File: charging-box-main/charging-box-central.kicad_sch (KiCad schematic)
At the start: 15 parts, among them J1 Accumulator 1, J10 mains power indicator, J11 Close AIRs, J2 Accumulator 2, J3 Main 12V, J4 Latching, J5 Charger, J6 IMD FAULT LED active low, J7 BMS LED active low, J8 Latching reset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

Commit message: mounting holes and rounded corners
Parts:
- added H1, H2, H3, H4: MountingHole_Pad, MountingHole:MountingHole_3.2mm_M3_DIN965_Pad_TopBottom, symbol Mechanical:MountingHole_Pad
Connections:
- net GND: now also H1.1, H2.1, H3.1, H4.1

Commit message: put the labels
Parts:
- R1, R2, R7: footprint Resistor_THT:R_Axial_DIN0207_L6.3mm_D2.5mm_P10.16mm_Horizontal -> Resistor_SMD:R_0805_2012Metric_Pad1.20x1.40mm_HandSolder
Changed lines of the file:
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@@
 			)
 		)
-		(property "Footprint" "Resistor_THT:R_Axial_DIN0207_L6.3mm_D2.5mm_P10.16mm_Horizontal"
+		(property "Footprint" "Resistor_SMD:R_0805_2012Metric_Pad1.20x1.40mm_HandSolder"
 			(at 125.095 134.112 90)
 			(effects
@@
 			)
 		)
-		(property "Footprint" "Resistor_THT:R_Axial_DIN0207_L6.3mm_D2.5mm_P10.16mm_Horizontal"
+		(property "Footprint" "Resistor_SMD:R_0805_2012Metric_Pad1.20x1.40mm_HandSolder"
 			(at 180.34 84.328 90)
 			(effects
@@
 			)
 		)
-		(property "Footprint" "Resistor_THT:R_Axial_DIN0207_L6.3mm_D2.5mm_P10.16mm_Horizontal"
+		(property "Footprint" "Resistor_SMD:R_0805_2012Metric_Pad1.20x1.40mm_HandSolder"
 			(at 180.34 91.313 90)
 			(effects

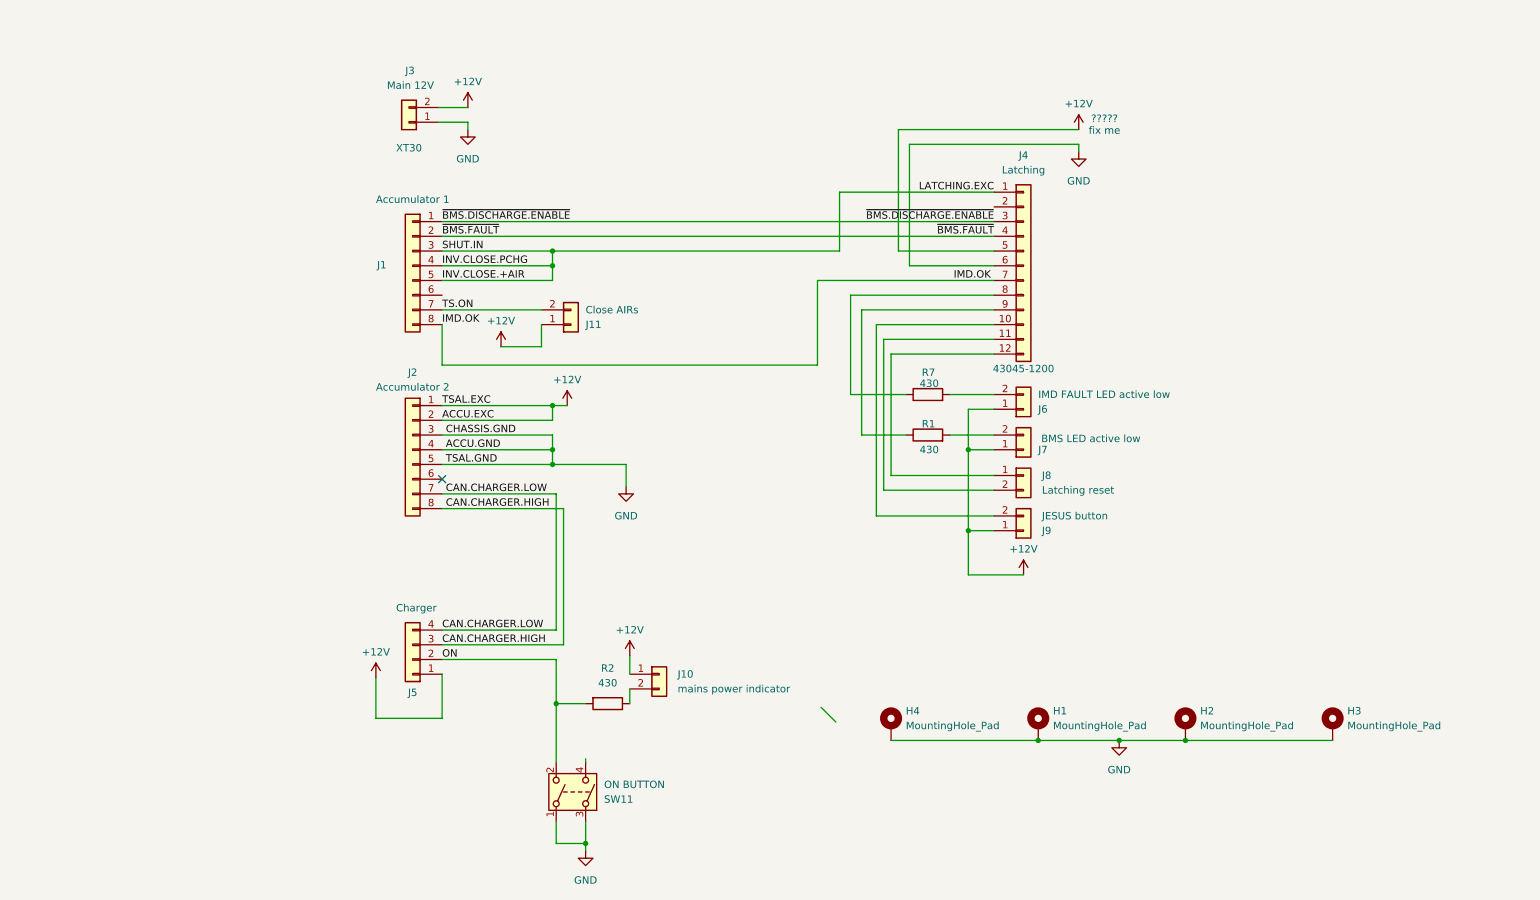
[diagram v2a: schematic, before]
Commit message: added fuses
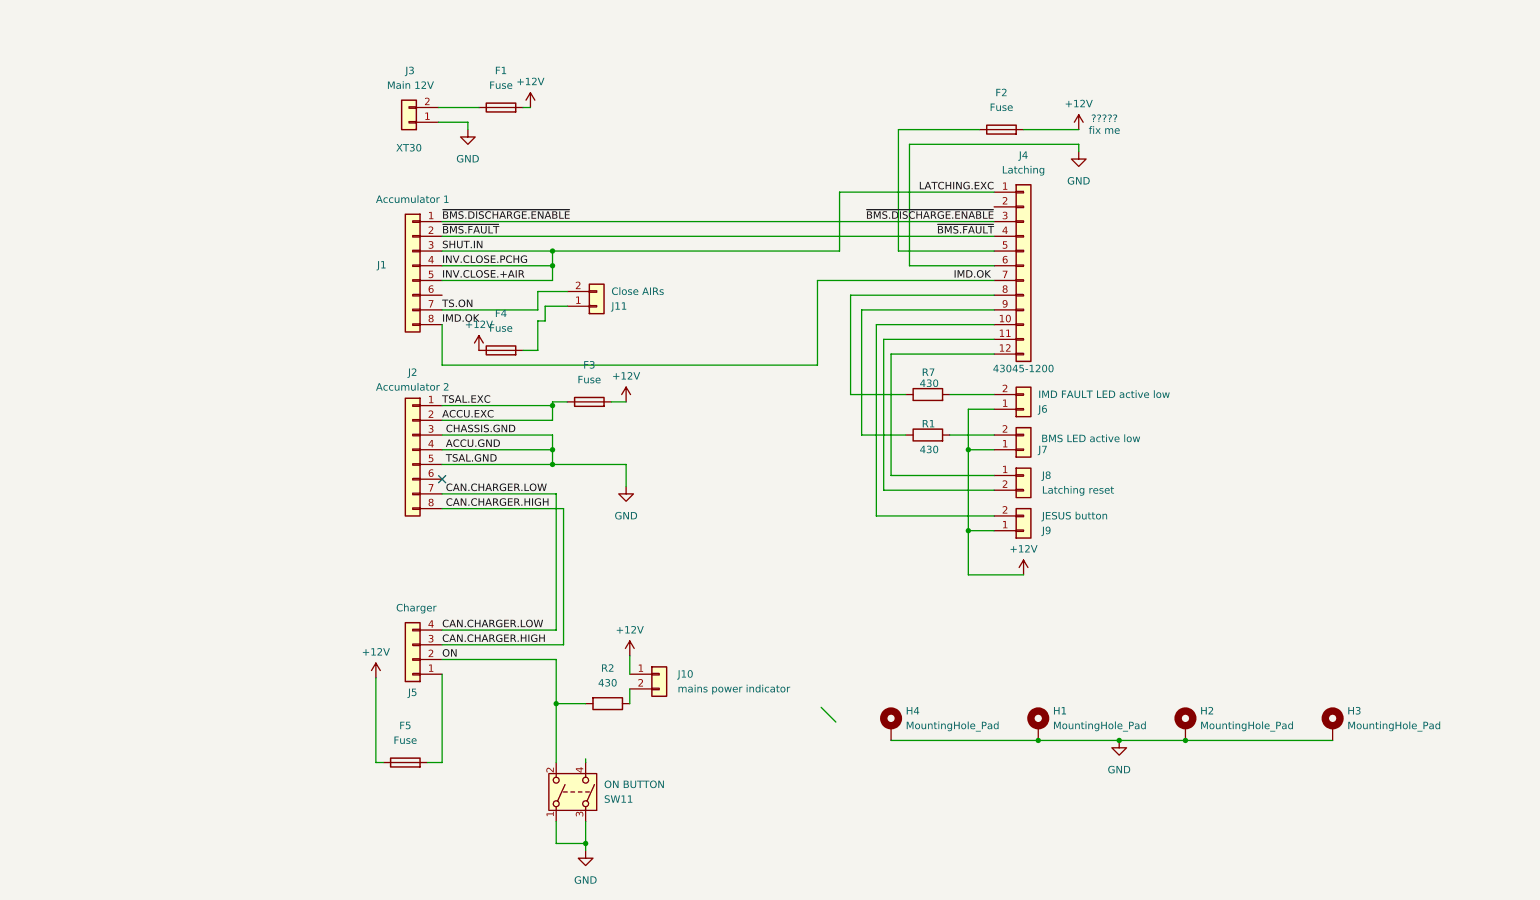
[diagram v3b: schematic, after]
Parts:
- added F1, F2, F3, F4, F5: Fuse, Fuse:Fuse_0603_1608Metric, symbol Device:Fuse
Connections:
- net +12V: now also F1.2, F2.2, F3.2, F4.1, F5.1; no longer J11.1 (Pin_1), J2.1 (Pin_1), J2.2 (Pin_2), J3.2 (Pin_2), J4.5 (Pin_5), J5.1 (Pin_1)
- new net: F2.1, J4.5 (Pin_5)
- new net: F4.2, J11.1 (Pin_1)
- new net: F5.2, J5.1 (Pin_1)
- new net: F1.1, J3.2 (Pin_2)
- new net ACCU.EXC: F3.1, J2.1 (Pin_1), J2.2 (Pin_2)
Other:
- moved on the sheet: J11

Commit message: made it a lill bit neater
not much
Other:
- note added: "????? fix me no"
- note removed: "????? fix me"
- moved on the sheet: F1, F2, F3, F4, F5, J1, J10, J11, J2, J3, J4, J5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

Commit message: routing fixes
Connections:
- net CAN.CHARGER.HIGH renamed CAN.CHARGER+
- net CAN.CHARGER.LOW renamed CAN.CHARGER-
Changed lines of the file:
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@@
 		)
 	)
-	(label "CAN.CHARGER.LOW"
+	(label "CAN.CHARGER-"
 		(at 67.31 98.425 0)
 		(effects
@@
 		)
 	)
-	(label "CAN.CHARGER.HIGH"
+	(label "CAN.CHARGER+"
 		(at 66.675 124.46 0)
 		(effects
@@
 		)
 	)
-	(label "CAN.CHARGER.LOW"
+	(label "CAN.CHARGER-"
 		(at 66.675 121.92 0)
 		(effects
@@
 		)
 	)
-	(label "CAN.CHARGER.HIGH"
+	(label "CAN.CHARGER+"
 		(at 67.31 100.965 0)
 		(effects

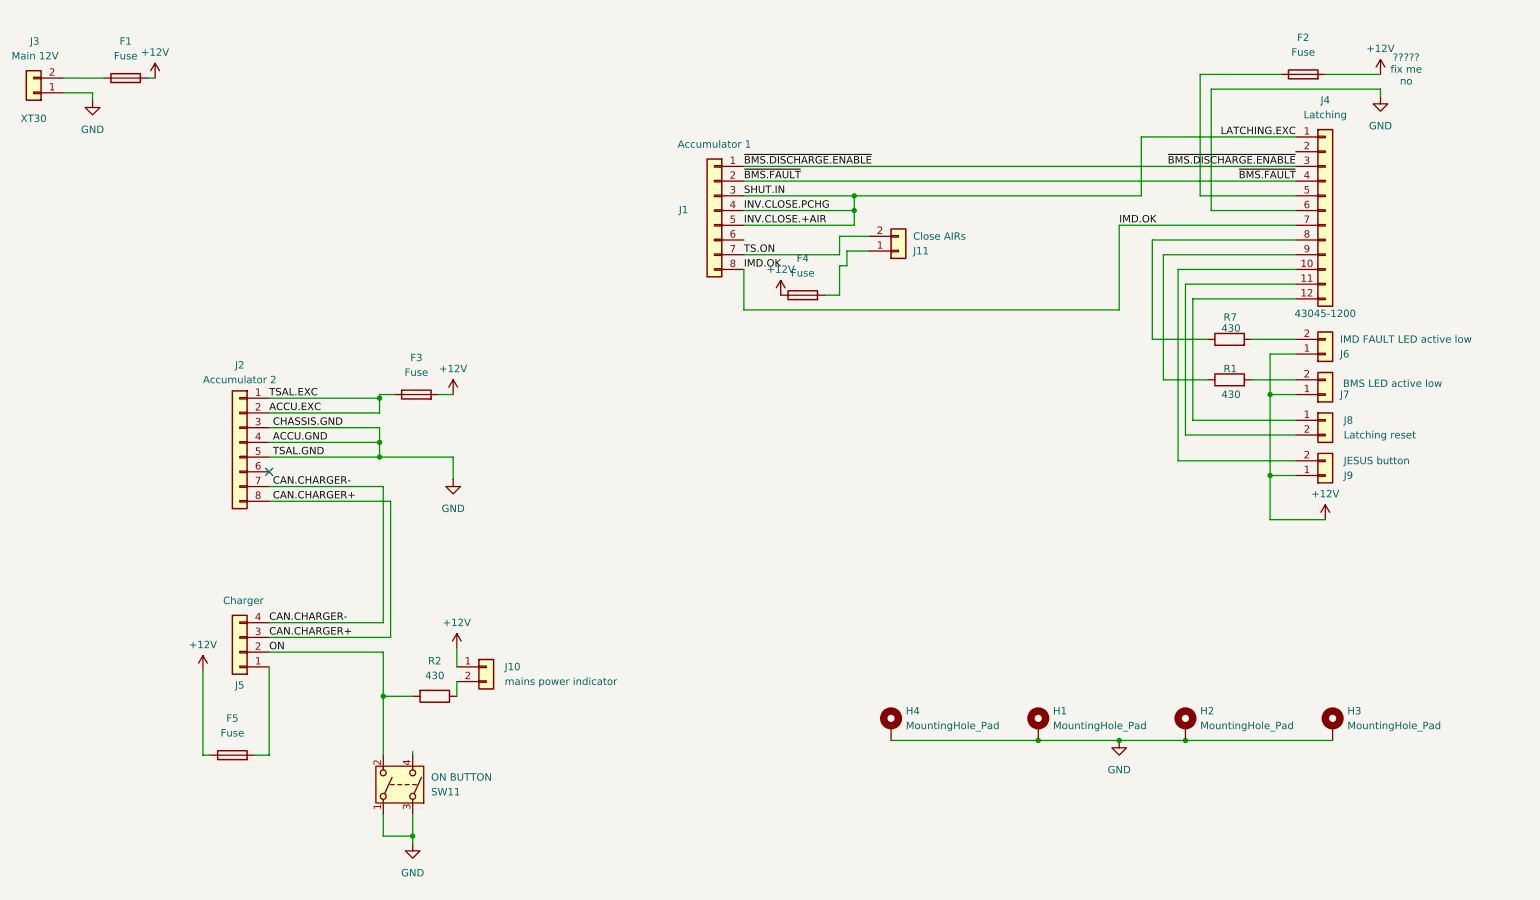
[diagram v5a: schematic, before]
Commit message: Sent pcb for production
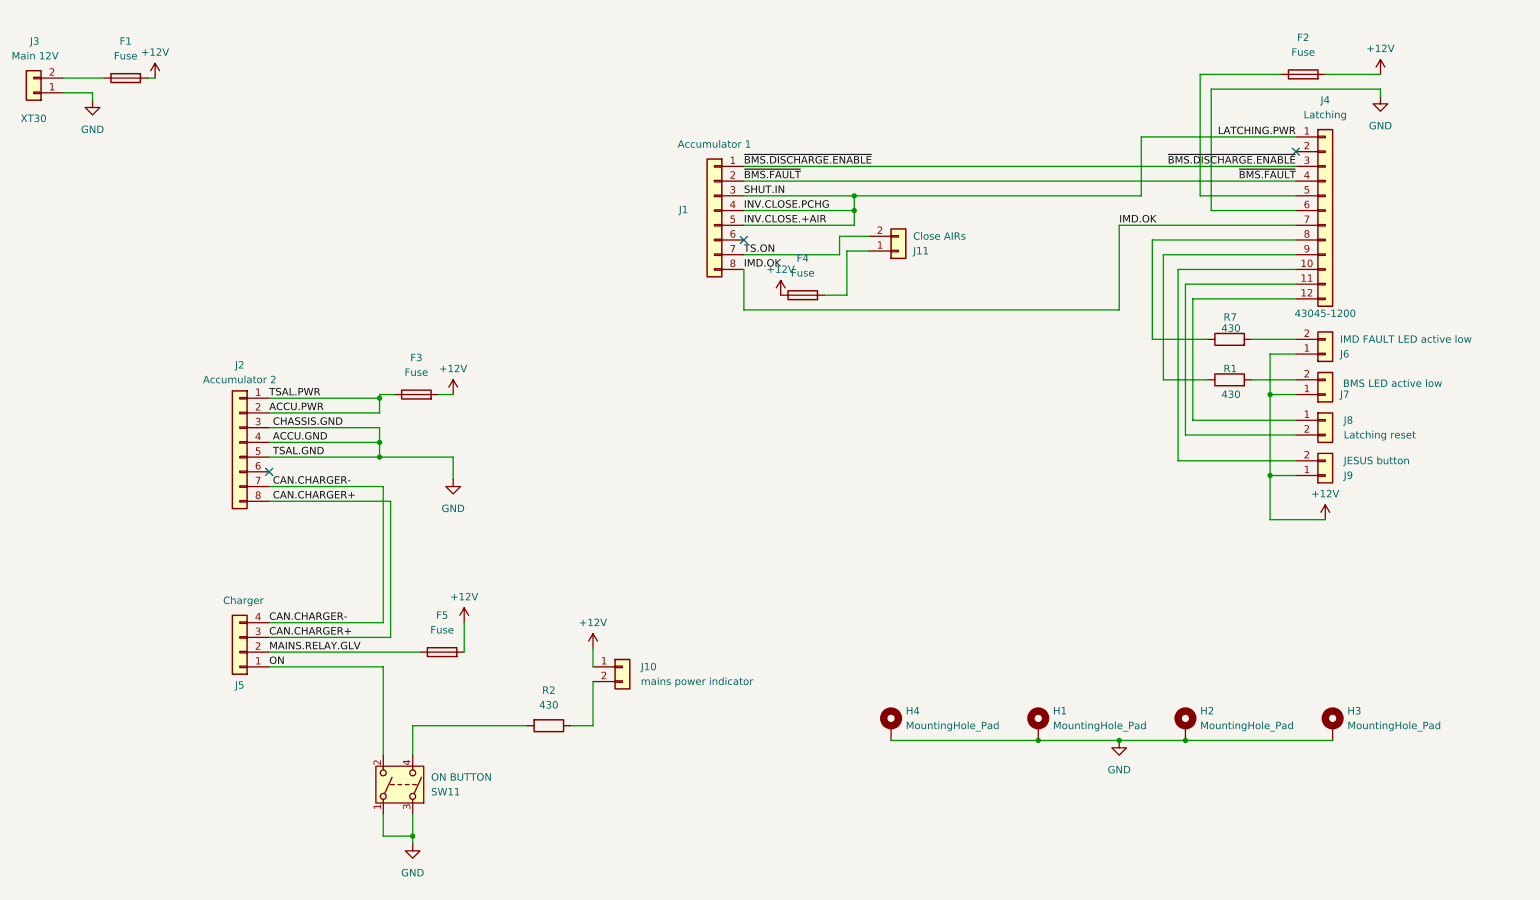
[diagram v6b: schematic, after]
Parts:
- SW11: footprint Connector_Molex:Molex_Micro-Fit_3.0_43045-0200_2x01_P3.00mm_Horizontal -> Connector_Molex:Molex_Micro-Fit_3.0_43045-0400_2x02_P3.00mm_Horizontal
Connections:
- net +12V: now also F5.2; no longer F5.1
- net ON: now also J5.1 (Pin_1); no longer J5.2 (Pin_2), R2.2
- net at SW11.4: now also R2.2
- net ACCU.EXC renamed ACCU.PWR
- new net MAINS.RELAY.GLV: F5.1, J5.2 (Pin_2)
- no-connect marks 1 -> 3
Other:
- note removed: "????? fix me no"
- moved on the sheet: F5, J10, R2

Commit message: Changes
Production on pause
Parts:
- removed F2: Fuse, Fuse:Fuse_0603_1608Metric, symbol Device:Fuse
- added J12: TSAL GREEN LED active high, Connector_Molex:Molex_Micro-Fit_3.0_43045-0200_2x01_P3.00mm_Horizontal, symbol Connector_Generic:Conn_01x02
- added R3: 430, Resistor_SMD:R_0805_2012Metric_Pad1.20x1.40mm_HandSolder, symbol Device:R
- J7: value BMS LED active low -> AMS LED active low
- J9: value JESUS button -> E-STOP
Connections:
- net +12V: now also J4.5 (Pin_5)
- net GND: now also J2.6 (Pin_6), J12.1 (Pin_1); no longer J2.3 (Pin_3)
- net LATCHING.RESET-: now reaches J4.12 (Pin_12), J8.1 (Pin_1)
- net LATCHING.RESET+: now reaches J4.11 (Pin_11), J8.2 (Pin_2)
- net SHUT.LATCHING: now reaches J4.10 (Pin_10), J9.2 (Pin_2)
- net IMD.FAULT.LATCHING: now reaches J4.8 (Pin_8), R7.1
- net AMS.FAULT.LATCHING: now reaches J4.9 (Pin_9), R1.1
- net TSAL.GREEN.LIGHT: now reaches J1.6 (Pin_6)
- net TSAL.GREEN.LIGHT: now also R3.1
- net ACCU.PWR renamed ACCU.CHARGE.PWR
- net ACCU.CHARGE.PWR: now also J2.3 (Pin_3)
- new net: J12.2 (Pin_2), R3.2
- no-connect marks 3 -> 1
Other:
- moved on the sheet: J11

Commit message: add mosfet for green light
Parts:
- added Q1: Q_PMOS-E_Generic_GSD, Package_TO_SOT_SMD:SOT-23, symbol PCM_Transistor_MOSFET_AKL:Q_PMOS-E_Generic_GSD
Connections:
- net +12V: now also Q1.2 (S)
- net TSAL.GREEN.LIGHT: now also Q1.3 (D); no longer J1.6 (Pin_6)
- new net: J1.6 (Pin_6), Q1.1 (G)
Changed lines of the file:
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@@
 	(wire
 		(pts
-			(xy 199.39 113.03) (xy 234.95 113.03)
-		)
-		(stroke
-			(width 0)
-			(type default)
-		)
-	)
-	(wire
-		(pts
 			(xy 243.84 63.5) (xy 224.79 63.5)
 		)
@@
 	(wire
 		(pts
-			(xy 199.39 55.88) (xy 199.39 113.03)
+			(xy 196.85 55.88) (xy 196.85 95.885)
 		)
 		(stroke
@@
 	(wire
 		(pts
+			(xy 205.74 113.03) (xy 205.74 102.235)
+		)
+		(stroke
+			(width 0)
+			(type default)
+		)
+	)
+	(wire
+		(pts
 			(xy 219.075 55.88) (xy 243.84 55.88)
 		)
@@
 	(wire
 		(pts
-			(xy 148.59 55.88) (xy 199.39 55.88)
+			(xy 148.59 55.88) (xy 196.85 55.88)
 		)
 		(stroke
@@
 	(wire
 		(pts
+			(xy 203.2 102.235) (xy 205.74 102.235)
+		)
+		(stroke
+			(width 0)
+			(type default)
+		)
+	)
+	(wire
+		(pts
 			(xy 224.79 142.24) (xy 250.19 142.24)
 		)
@@
 	(wire
 		(pts
+			(xy 183.515 99.06) (xy 183.515 102.235)
+		)
+		(stroke
+			(width 0)
+			(type default)
+		)
+	)
+	(wire
+		(pts
 			(xy 148.59 48.26) (xy 167.64 48.26)
 		)
@@
 	(wire
 		(pts
+			(xy 183.515 102.235) (xy 193.04 102.235)
+		)
+		(stroke
+			(width 0)
+			(type default)
+		)
+	)
+	(wire
+		(pts
 			(xy 148.59 60.96) (xy 148.59 67.945)
 		)
@@
 	(wire
 		(pts
+			(xy 205.74 113.03) (xy 234.95 113.03)
+		)
+		(stroke
+			(width 0)
+			(type default)
+		)
+	)
+	(wire
+		(pts
 			(xy 213.36 142.24) (xy 224.79 142.24)
 		)
@@
 		)
 	)
-	(label "TSAL.GREEN.LIGHT"
-		(at 148.59 55.88 0)
-		(effects
-			(font
-				(size 1.27 1.27)
-			)
-			(justify left bottom)
-		)
-	)
 	(label "CAN.CHARGER+"
 		(at 66.675 124.46 0)
@@
 	)
 	(symbol
+		(lib_id "PCM_Transistor_MOSFET_AKL:Q_PMOS-E_Generic_GSD")
+		(at 198.12 99.695 90)
+		(mirror x)
+		(unit 1)
+		(exclude_from_sim no)
+		(in_bom yes)
+		(on_board yes)
+		(dnp no)
+		(property "Reference" "Q1"
+			(at 198.12 106.045 90)
+			(effects
+				(font
+					(size 1.27 1.27)
+				)
+			)
+		)
+		(property "Value" "Q_PMOS-E_Generic_GSD"
+			(at 198.12 108.585 90)
+			(effects
+				(font
+					(size 1.27 1.27)
+				)
+			)
+		)
+		(property "Footprint" "Package_TO_SOT_SMD:SOT-23"
+			(at 200.66 104.775 0)
+			(effects
+				(font
+					(size 1.27 1.27)
+				)
+				(hide yes)
+			)
+		)
+		(property "Datasheet" "~"
+			(at 198.12 99.695 0)
+			(effects
+				(font
+					(size 1.27 1.27)
+				)
+				(hide yes)
+			)
+		)
+		(property "Description" "P-MOSFET enchancement mode transistor, generic symbol, Alternate KiCAD Library"
+			(at 198.12 99.695 0)
+			(effects
+				(font
+					(size 1.27 1.27)
+				)
+				(hide yes)
+			)
+		)
+		(pin "3"
+		)
+		(pin "2"
+		)
+		(pin "1"
+		)
+		(instances
+			(project ""
+				(path "/58f30d17-2e70-48b3-883a-be84a394a8cc"
+					(reference "Q1")
+					(unit 1)
+				)
+			)
+		)
+	)
+	(symbol
 		(lib_id "power:GND")
 		(at 243.84 122.555 0)
@@
 					(unit 1)
 				)
+			)
+		)
+	)
+	(symbol
+		(lib_id "power:+12V")
+		(at 183.515 99.06 0)
+		(unit 1)
+		(exclude_from_sim no)
+		(in_bom yes)
+		(on_board yes)
+		(dnp no)
+		(fields_autoplaced yes)
+		(property "Reference" "#PWR014"
+			(at 183.515 102.87 0)
+			(effects
+				(font
+					(size 1.27 1.27)
+				)
+				(hide yes)
+			)
+		)
+		(property "Value" "+12V"
+			(at 183.515 94.615 0)
+			(effects
+				(font
+					(size 1.27 1.27)
+				)
+			)
+		)
+		(property "Footprint" ""
+			(at 183.515 99.06 0)
+			(effects
+				(font
+					(size 1.27 1.27)
+				)
+				(hide yes)
+			)
+		)
+		(property "Datasheet" ""
+			(at 183.515 99.06 0)
+			(effects
+				(font
+					(size 1.27 1.27)
+				)
+				(hide yes)
+			)
+		)
+		(property "Description" "Power symbol creates a global label with name \"+12V\""
+			(at 183.515 99.06 0)
+			(effects
+				(font
+					(size 1.27 1.27)
+				)
+				(hide yes)
+			)
+		)
+		(pin "1"
+		)
+		(instances
+			(project "charging-box-central"
+				(path "/58f30d17-2e70-48b3-883a-be84a394a8cc"
+					(reference "#PWR014")
+					(unit 1)
+				)
